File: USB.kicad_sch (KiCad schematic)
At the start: 35 parts, among them J11 USB3_A, J12 USB3_A, U16 USB5744_2G, U8 AP22653W6, Y5 25Mhz

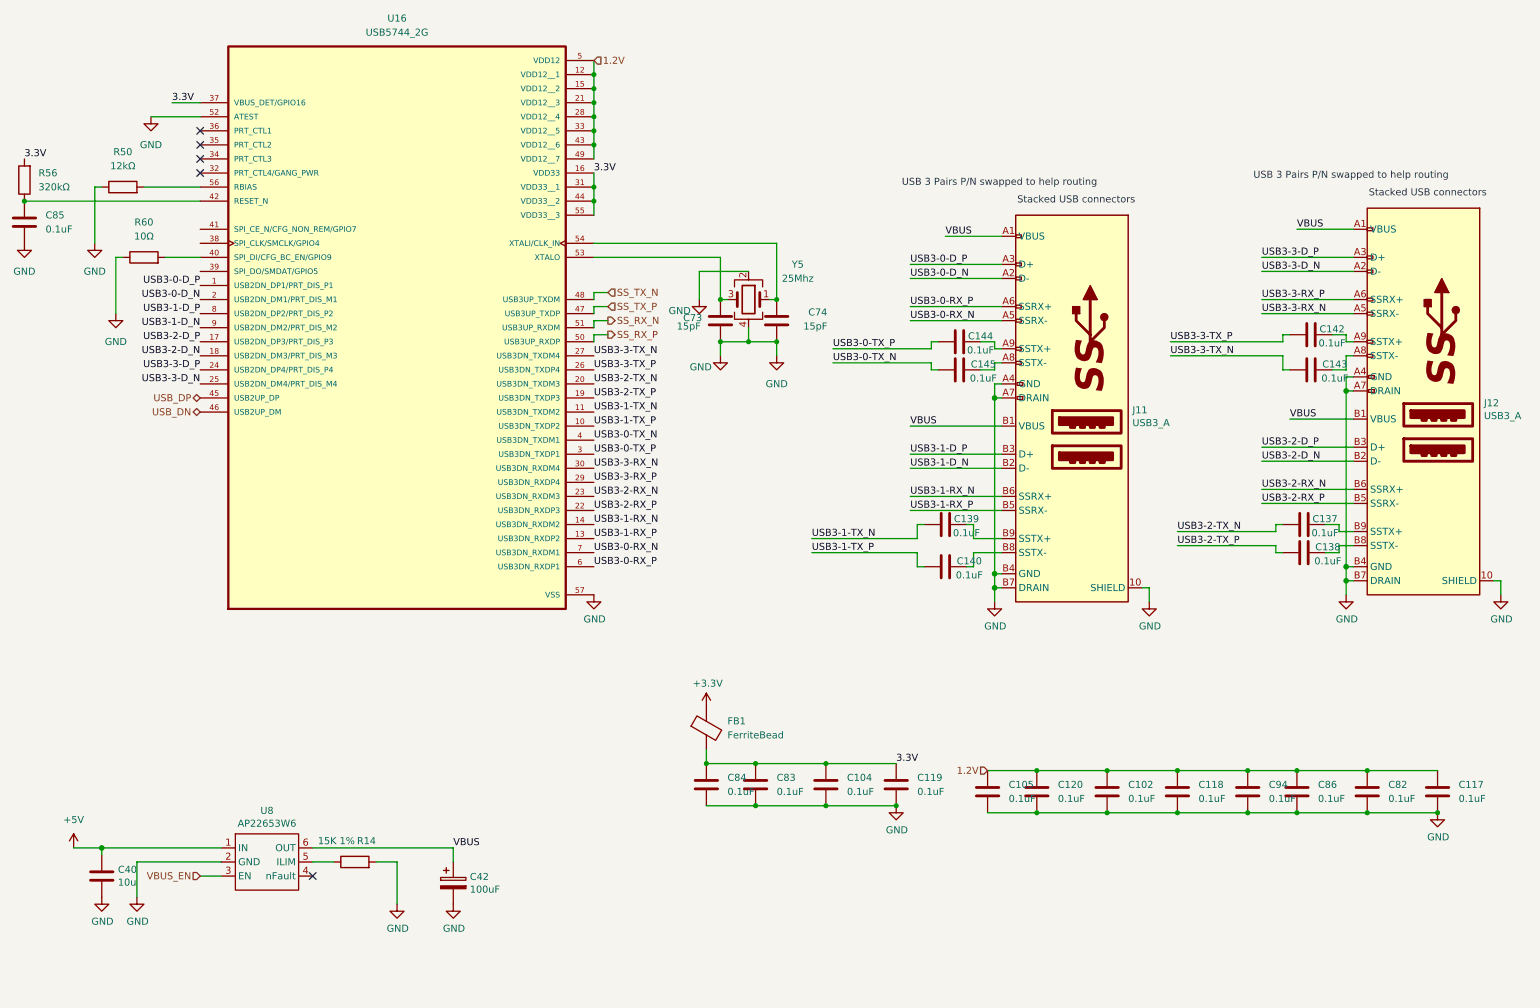
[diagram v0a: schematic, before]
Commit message: delete usb hub
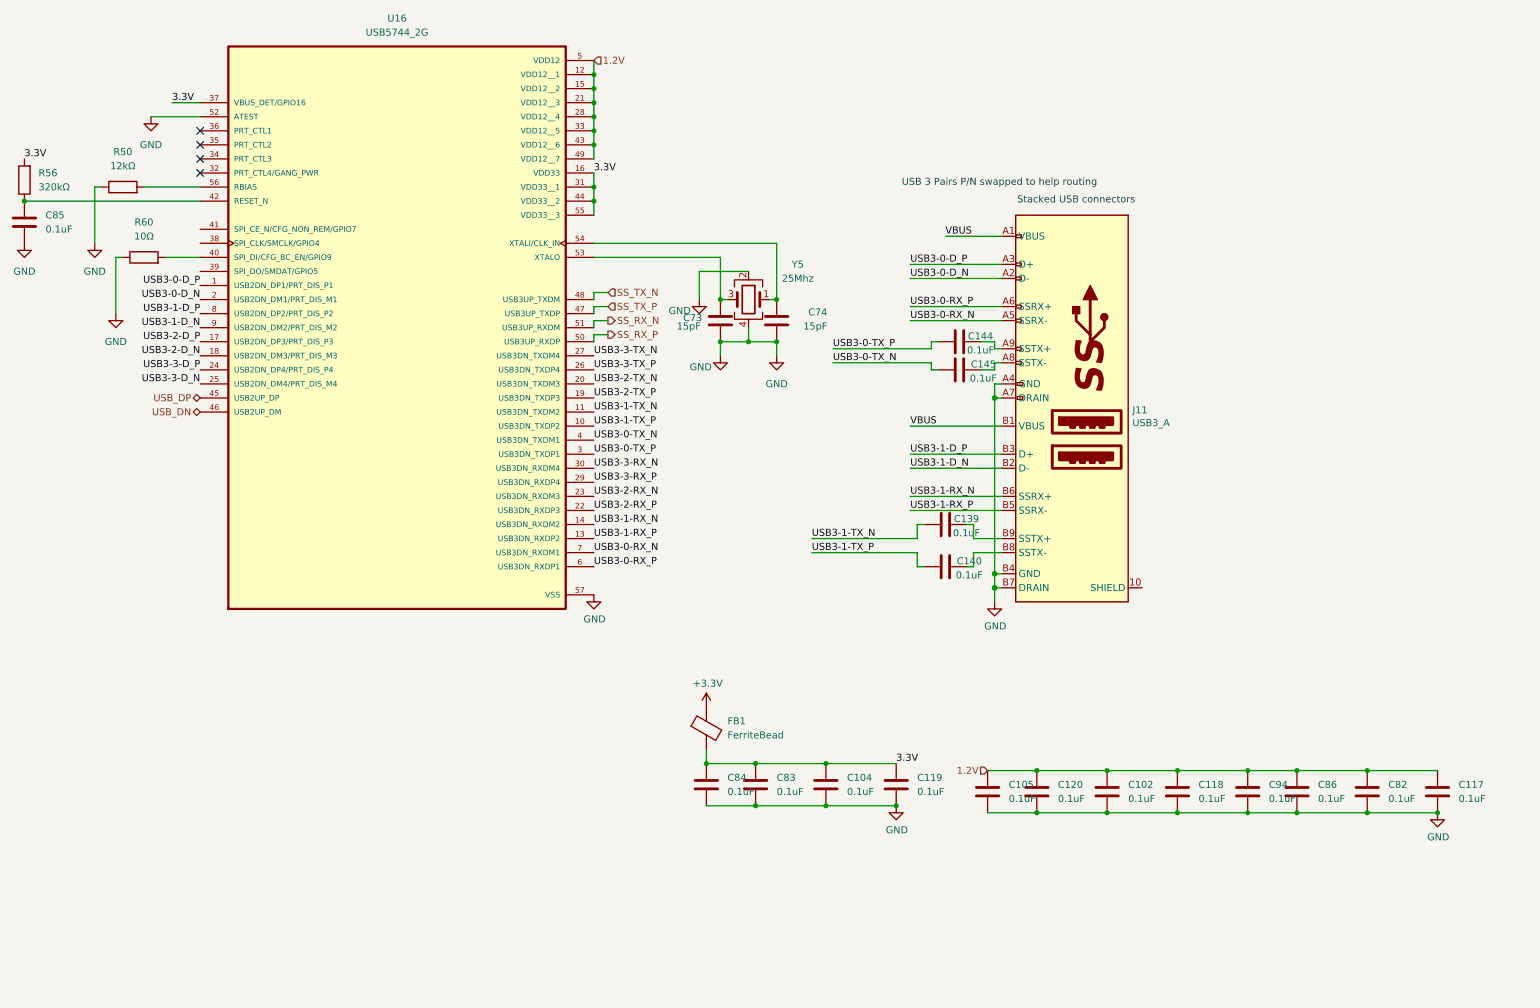
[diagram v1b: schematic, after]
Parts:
- removed C137, C138, C142, C143: 0.1uF, Capacitor_SMD:C_0402_1005Metric_Pad0.74x0.62mm_HandSolder, symbol Device:C
- removed C40: 10u, Capacitor_SMD:C_0805_2012Metric, symbol Device:C
- removed C42: 100uF, Capacitor_Tantalum_SMD:CP_EIA-7343-31_Kemet-D, symbol Device:C_Polarized
- removed J12: USB3_A, CM5IO:MTCONN_UBAF30-D2011, symbol CM5IO:USB3_A
- removed R14: 15K 1%, Resistor_SMD:R_0603_1608Metric_Pad0.98x0.95mm_HandSolder, symbol Device:R
- removed U8: AP22653W6, Package_TO_SOT_SMD:SOT-23-6, symbol CM5IO:AP2553W6
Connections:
- net GND: no longer J11.10 (SHIELD)
- no-connect marks 5 -> 4

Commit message: データをアップロード
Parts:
- removed C102, C104, C105, C117, C118, C119, C120, C139, C140, C144, C145, C82, C83, C84, C85, C86, C94: 0.1uF, Capacitor_SMD:C_0402_1005Metric_Pad0.74x0.62mm_HandSolder, symbol Device:C
- removed C73, C74: 15pF, Capacitor_SMD:C_0603_1608Metric_Pad1.08x0.95mm_HandSolder, symbol Device:C
- removed FB1: FerriteBead, Inductor_SMD:L_0603_1608Metric_Pad1.05x0.95mm_HandSolder, symbol Device:FerriteBead
- removed J11: USB3_A, CM5IO:MTCONN_UBAF30-D2011, symbol CM5IO:USB3_A
- removed R50: 12kΩ, Resistor_SMD:R_0603_1608Metric_Pad0.98x0.95mm_HandSolder, symbol Device:R
- removed R56: 320kΩ, Resistor_SMD:R_0603_1608Metric, symbol Device:R
- removed R60: 10Ω, Resistor_SMD:R_0603_1608Metric, symbol Device:R
- removed U16: USB5744_2G, CM5IO:VQFN56_2G_MCH, symbol USB5744:USB5744_2G
- removed Y5: 25Mhz, Crystal:Crystal_SMD_SeikoEpson_FA128-4Pin_2.0x1.6mm, symbol Device:Crystal_GND24
- added C106, C107, C108: 0.1u, Capacitor_SMD:C_0402_1005Metric_Pad0.74x0.62mm_HandSolder, symbol Device:C
- added C40: 10u, Capacitor_SMD:C_0805_2012Metric, symbol Device:C
- added C42: 100uF, Capacitor_Tantalum_SMD:CP_EIA-7343-31_Kemet-D, symbol Device:C_Polarized
- added J12: USB3_A, CM5IO:MTCONN_UBAF30-D2011, symbol CM5IO:USB3_A
- added J8: USB_A_Stacked, Connector_USB:USB_A_Wuerth_61400826021_Horizontal_Stacked, symbol Connector:USB_A_Stacked
- added R7: 15K 1%, Resistor_SMD:R_0603_1608Metric_Pad0.98x0.95mm_HandSolder, symbol Device:R
- added U17: SL2.1A, Package_SO:SOIC-16_4.55x10.3mm_P1.27mm, symbol SL2.1A:SL2.1A
- added U7: AP22653W6, Package_TO_SOT_SMD:SOT-23-6, symbol CM5IO:AP2553W6
- added Y4: 12Mhz, Crystal:Resonator_SMD_Murata_CSTxExxV-3Pin_3.0x1.1mm, symbol Device:Resonator
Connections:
- net GND: now also C106.2, C107.2, C108.2, C40.2, C42.2, J12.10 (SHIELD), J12.A4 (GND), J12.A7 (DRAIN), J12.B4 (GND), J12.B7 (DRAIN), J8.4 (GND1), J8.8 (GND2), J8.9 (Shield), R7.2, U17.12 (GND), U7.2 (GND), Y4.2
- net VBUS: now also C106.1, C42.1, J12.A1 (VBUS), J12.B1 (VBUS), J8.1 (VBUS1), J8.5 (VBUS2), U17.11 (VCC5V), U7.6 (OUT)
- new net: U17.15 (XOUT), Y4.1
- new net: U17.16 (XIN), Y4.3
- new net: C108.1, U17.14 (VDD18)
- new net: C107.1, U17.13 (VDD3)
- new net: R7.1, U7.5 (ILIM)
- new net +5V: C40.1, U7.1 (IN)
- new net D3N: J8.6 (D2-), U17.3 (DM3)
- new net D3P: J8.7 (D2+), U17.4 (DP3)
- new net D4N: J8.2 (D1-), U17.1 (DM4)
- new net D4P: J8.3 (D1+), U17.2 (DP4)
- new net MCU.DN: U17.7 (DM1)
- new net MCU.DP: U17.8 (DP1)
- new net USB0.DN: J12.B2 (D-)
- new net USB0.DP: J12.B3 (D+)
- new net USB0.RXN: J12.B5 (SSRX-)
- new net USB0.RXP: J12.B6 (SSRX+)
- new net USB0.TXN: J12.B8 (SSTX-)
- new net USB0.TXP: J12.B9 (SSTX+)
- new net USB1.DN: J12.A2 (D-)
- new net USB1.DP: J12.A3 (D+)
- new net USB1.RXN: J12.A5 (SSRX-)
- new net USB1.RXP: J12.A6 (SSRX+)
- new net USB1.TXN: J12.A8 (SSTX-)
- new net USB1.TXP: J12.A9 (SSTX+)
- new net USB2.DN: U17.9 (UDM)
- new net USB2.DP: U17.10 (UDP)
- new net VBUS_EN: U7.3 (EN)
- new net WiFi.DN: U17.5 (DM2)
- new net WiFi.DP: U17.6 (DP2)
- no-connect marks 4 -> 1
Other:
- note added: "USB Switch"
- note added: "USB2.0 HUB"
- note added: "USB2.0 stack connector"
- note added: "USB3.0 stack connector"
- note removed: "Stacked USB connectors"
- note removed: "USB 3 Pairs P/N swapped to help routing"
